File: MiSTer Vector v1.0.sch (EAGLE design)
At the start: 35 parts, among them CON2 22-23-2021, IC2 TL084, IC3 TL084, IC7 MAX6105, U1 MCP4922, U2 MCP4922, U3 MCP4922, U8 VASD1-SIP

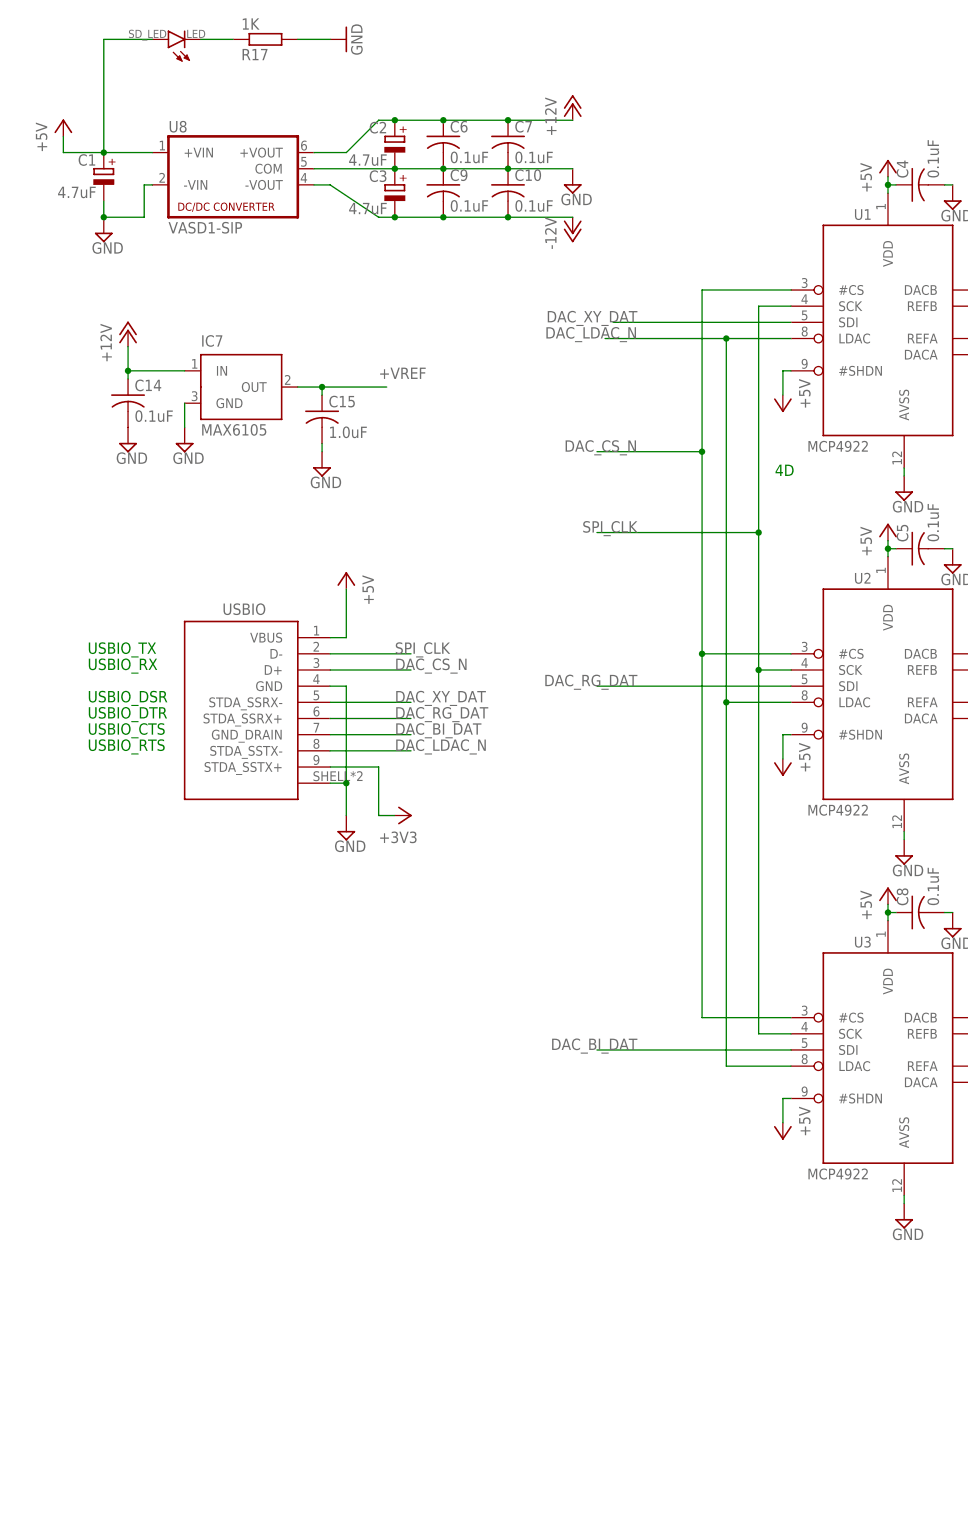
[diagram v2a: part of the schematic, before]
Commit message: added 3-pin VESA miniDIN, for 3D glasses
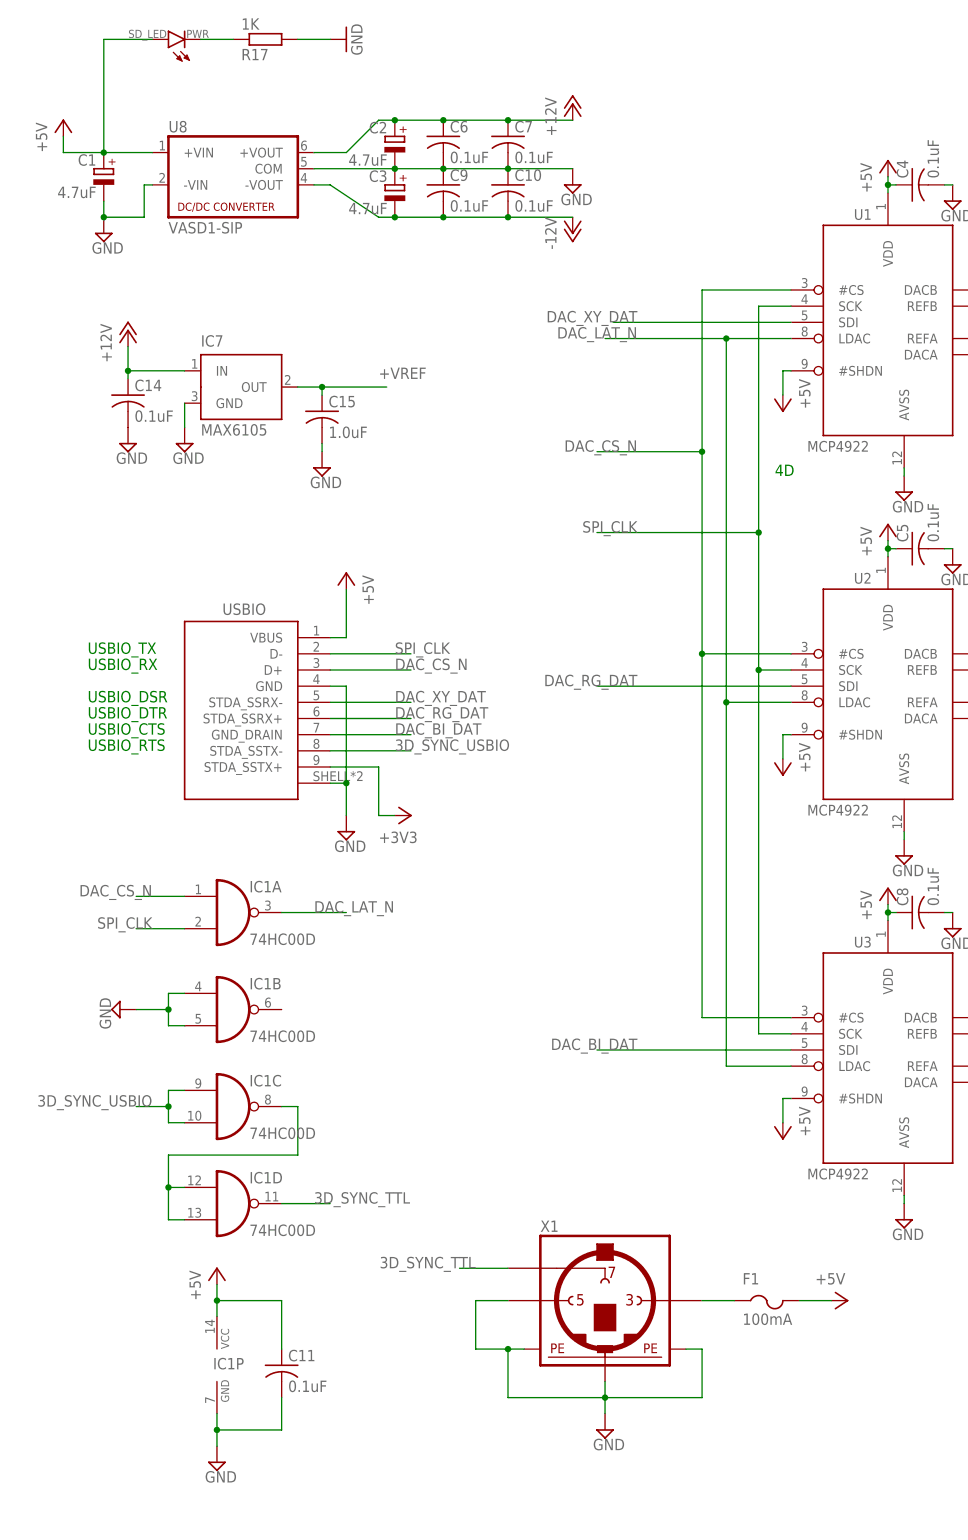
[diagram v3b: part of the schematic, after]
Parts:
- added C11: 0.1uF, adafruit:C-USC0603
- added F1: 100mA, adafruit:PTCFUSE-1206
- added IC1: 74HC00D, 74xx-eu:74HC00D
- added X1: (no value), mini_din:MINI_DIN_3
- renumbered LED to PWR
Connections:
- removed net DAC_LDAC_N: U1.LDAC, U2.LDAC, U3.LDAC, USBIO.STDA_SSTX-
- new net 3D_SYNC_TTL: IC1D.O, X1.7
- new net 3D_SYNC_USBIO: IC1C.I0, IC1C.I1, USBIO.STDA_SSTX-
- new net DAC_LAT_N: IC1A.O, U1.LDAC, U2.LDAC, U3.LDAC
- new net N$6: F1.1, X1.3
- new net N$8: IC1C.O, IC1D.I0, IC1D.I1
- net +5V: now also C11.1, F1.2, IC1P.VCC
- net DAC_CS_N: now also IC1A.I0
- net GND: now also C11.2, IC1B.I0, IC1B.I1, IC1P.GND, X1.5, X1.PE1, X1.PE2, X1.PE3
- net SPI_CLK: now also IC1A.I1

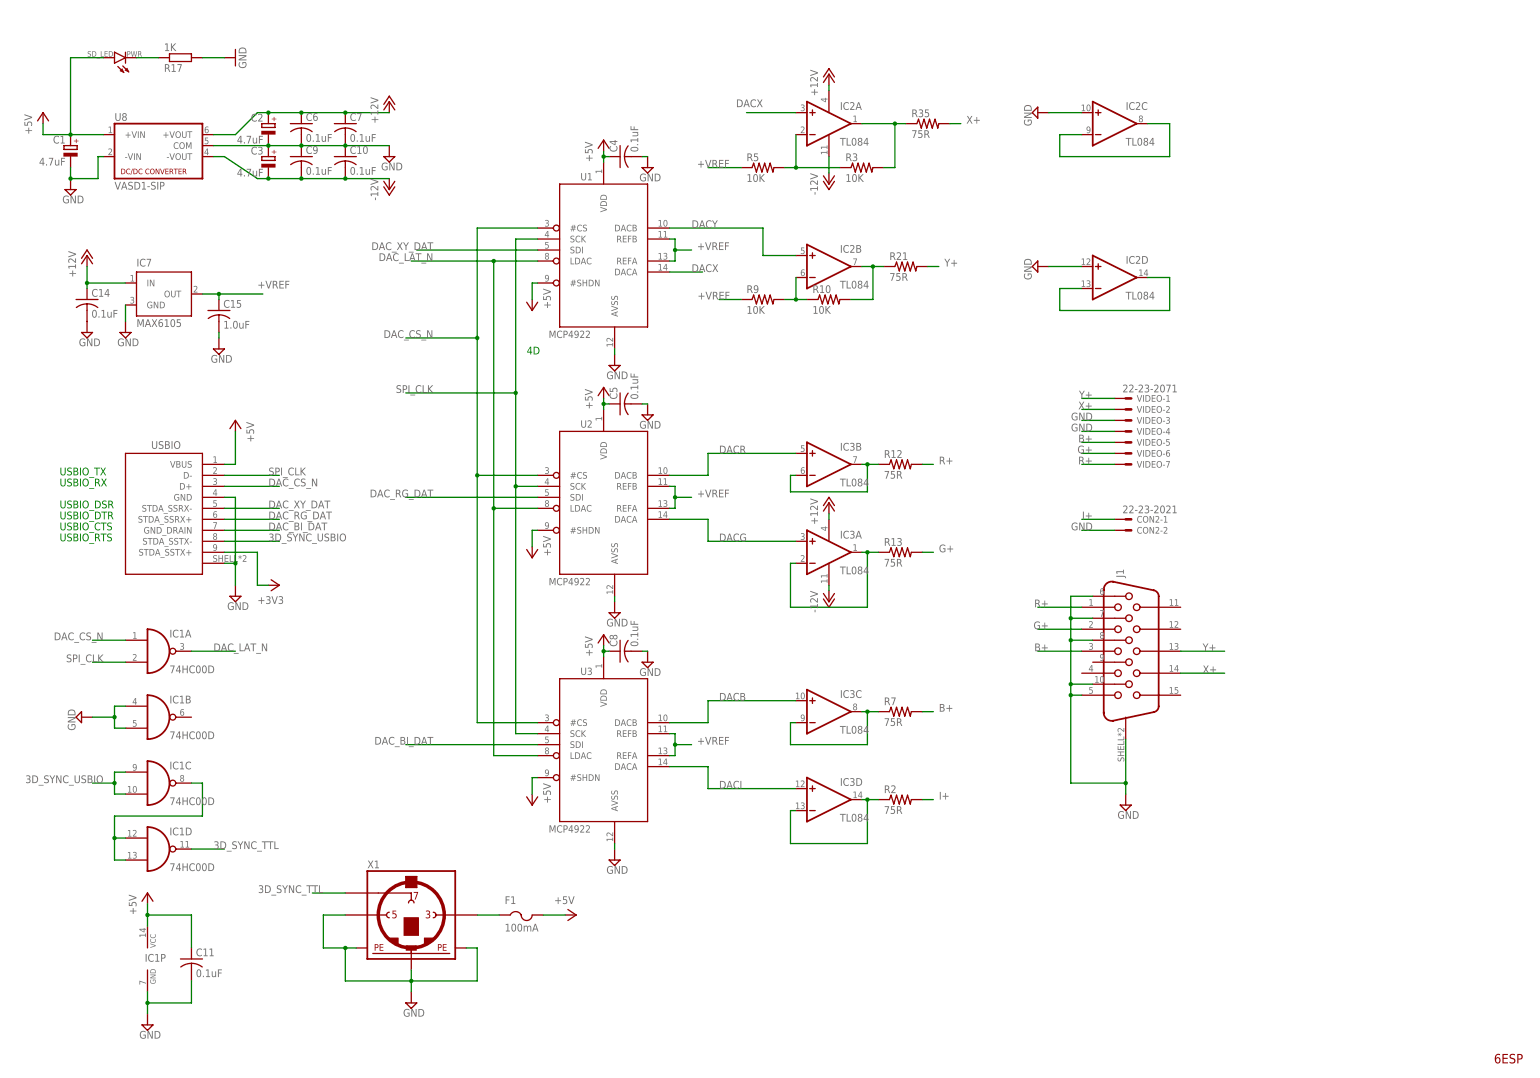
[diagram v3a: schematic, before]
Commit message: swapped two USBIO pins, for better signal integrity
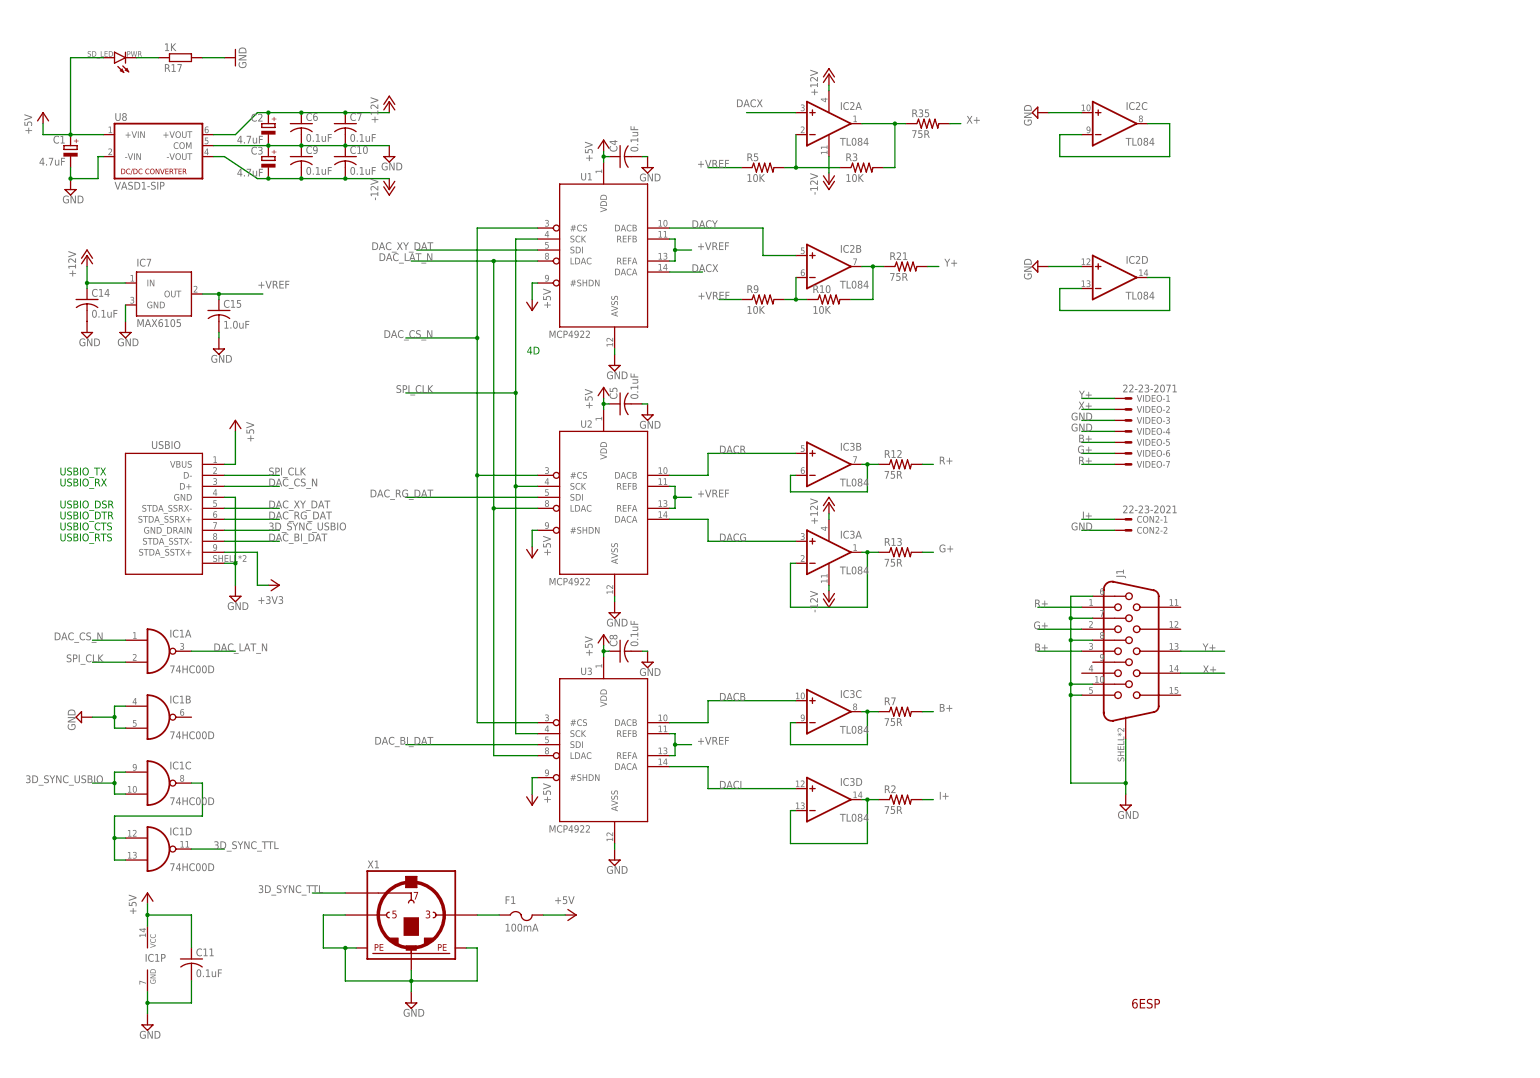
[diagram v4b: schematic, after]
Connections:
- net 3D_SYNC_USBIO: now also USBIO.GND_DRAIN; no longer USBIO.STDA_SSTX-
- net DAC_BI_DAT: now also USBIO.STDA_SSTX-; no longer USBIO.GND_DRAIN
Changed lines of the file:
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@@
 <sheet>
 <plain>
-<text x="252.73" y="-59.69" size="2.1844" layer="94">6ESP</text>
+<text x="168.91" y="-46.99" size="2.1844" layer="94">6ESP</text>
 <text x="29.21" y="104.14" size="1.778" layer="91">4D</text>
 <text x="-78.74" y="76.2" size="1.778" layer="91">USBIO_TX</text>
@@
 </plain>
 <instances>
-<instance part="FRAME1" gate="G$2" x="163.83" y="-67.31" smashed="yes">
-<attribute name="LAST_DATE_TIME" x="176.53" y="-66.04" size="2.54" layer="94" font="vector"/>
-<attribute name="SHEET" x="250.19" y="-66.04" size="2.54" layer="94" font="vector"/>
-<attribute name="DRAWING_NAME" x="181.61" y="-48.26" size="2.54" layer="94" font="vector"/>
+<instance part="FRAME1" gate="G$2" x="80.01" y="-54.61" smashed="yes">
+<attribute name="LAST_DATE_TIME" x="92.71" y="-53.34" size="2.54" layer="94" font="vector"/>
+<attribute name="SHEET" x="166.37" y="-53.34" size="2.54" layer="94" font="vector"/>
+<attribute name="DRAWING_NAME" x="97.79" y="-35.56" size="2.54" layer="94" font="vector"/>
 </instance>
 <instance part="U8" gate="G$1" x="-55.88" y="152.4"/>
@@
 </segment>
 <segment>
-<pinref part="USBIO" gate="G$1" pin="GND_DRAIN"/>
-<wire x1="-40.64" y1="63.5" x2="-27.94" y2="63.5" width="0.1524" layer="91"/>
-<label x="-30.48" y="63.5" size="1.778" layer="95"/>
+<pinref part="USBIO" gate="G$1" pin="STDA_SSTX-"/>
+<wire x1="-40.64" y1="60.96" x2="-27.94" y2="60.96" width="0.1524" layer="91"/>
+<label x="-30.48" y="60.96" size="1.778" layer="95"/>
 </segment>
 </net>
@@
 </net>
 <net name="3D_SYNC_USBIO" class="0">
-<segment>
-<pinref part="USBIO" gate="G$1" pin="STDA_SSTX-"/>
-<wire x1="-40.64" y1="60.96" x2="-27.94" y2="60.96" width="0.1524" layer="91"/>
-<label x="-30.48" y="60.96" size="1.778" layer="95"/>
-</segment>
 <segment>
 <pinref part="IC1" gate="C" pin="I0"/>
@@
 <label x="-68.58" y="5.08" size="1.778" layer="95" rot="MR0"/>
 </segment>
-</net>
+<segment>
+<pinref part="USBIO" gate="G$1" pin="GND_DRAIN"/>
+<wire x1="-40.64" y1="63.5" x2="-27.94" y2="63.5" width="0.1524" layer="91"/>
+<label x="-30.48" y="63.5" size="1.778" layer="95"/>
+</segment>
+</net>
